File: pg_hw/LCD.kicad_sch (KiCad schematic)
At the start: 28 parts, among them J2 FPC_Touch, J3 FPC_Display, U10 ttp233, U11 ttp233, U8 ttp233, U9 TTP233

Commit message: update ttp
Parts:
- removed R17, R18, R19, R20, R21, R22, R23, R24: R, Resistor_SMD:R_0402_1005Metric, symbol Device:R
- C12, C16, C18: value C -> 100u
- C13, C15, C17, C7: value C -> 22pF
- C14: value C -> 100uF
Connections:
- net GND: now also U10.4 (AHLB), U10.6 (TOG), U11.4 (AHLB), U11.6 (TOG), U8.4 (AHLB), U8.6 (TOG), U9.4 (AHLB), U9.6 (TOG)
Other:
- moved on the sheet: C12, C14, C16, C18

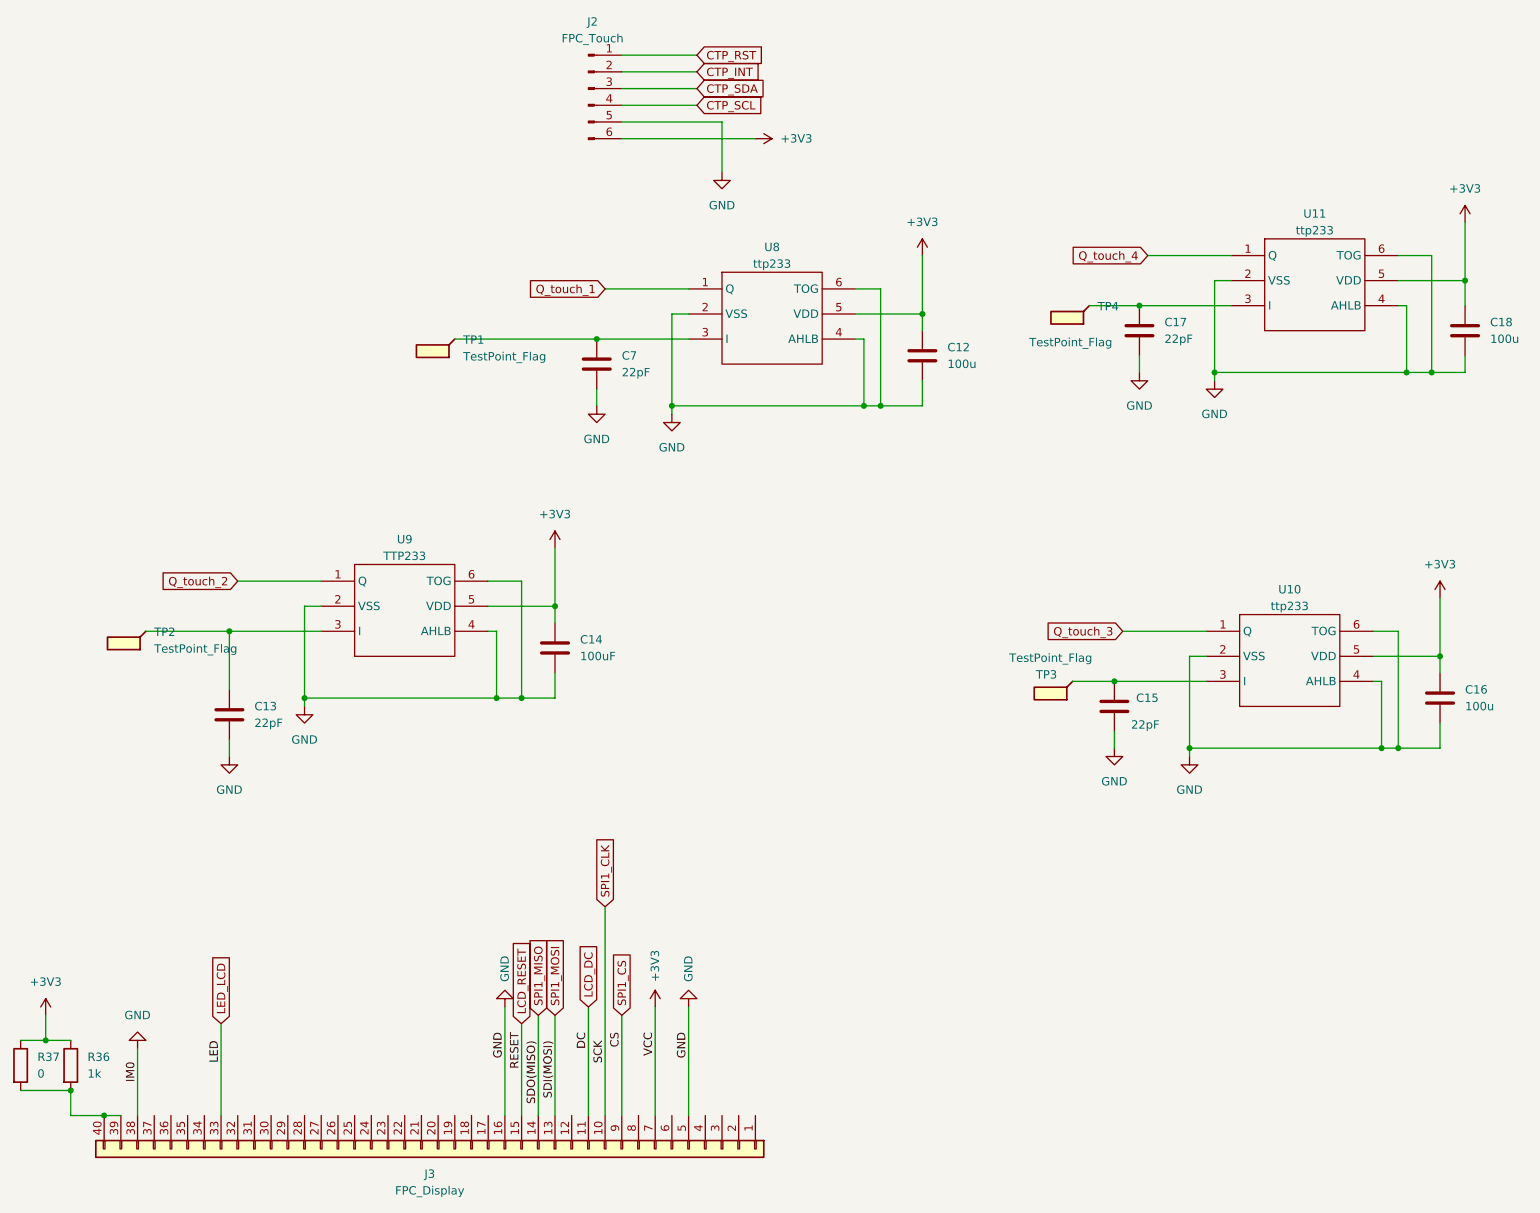
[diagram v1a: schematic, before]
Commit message: update touch pad
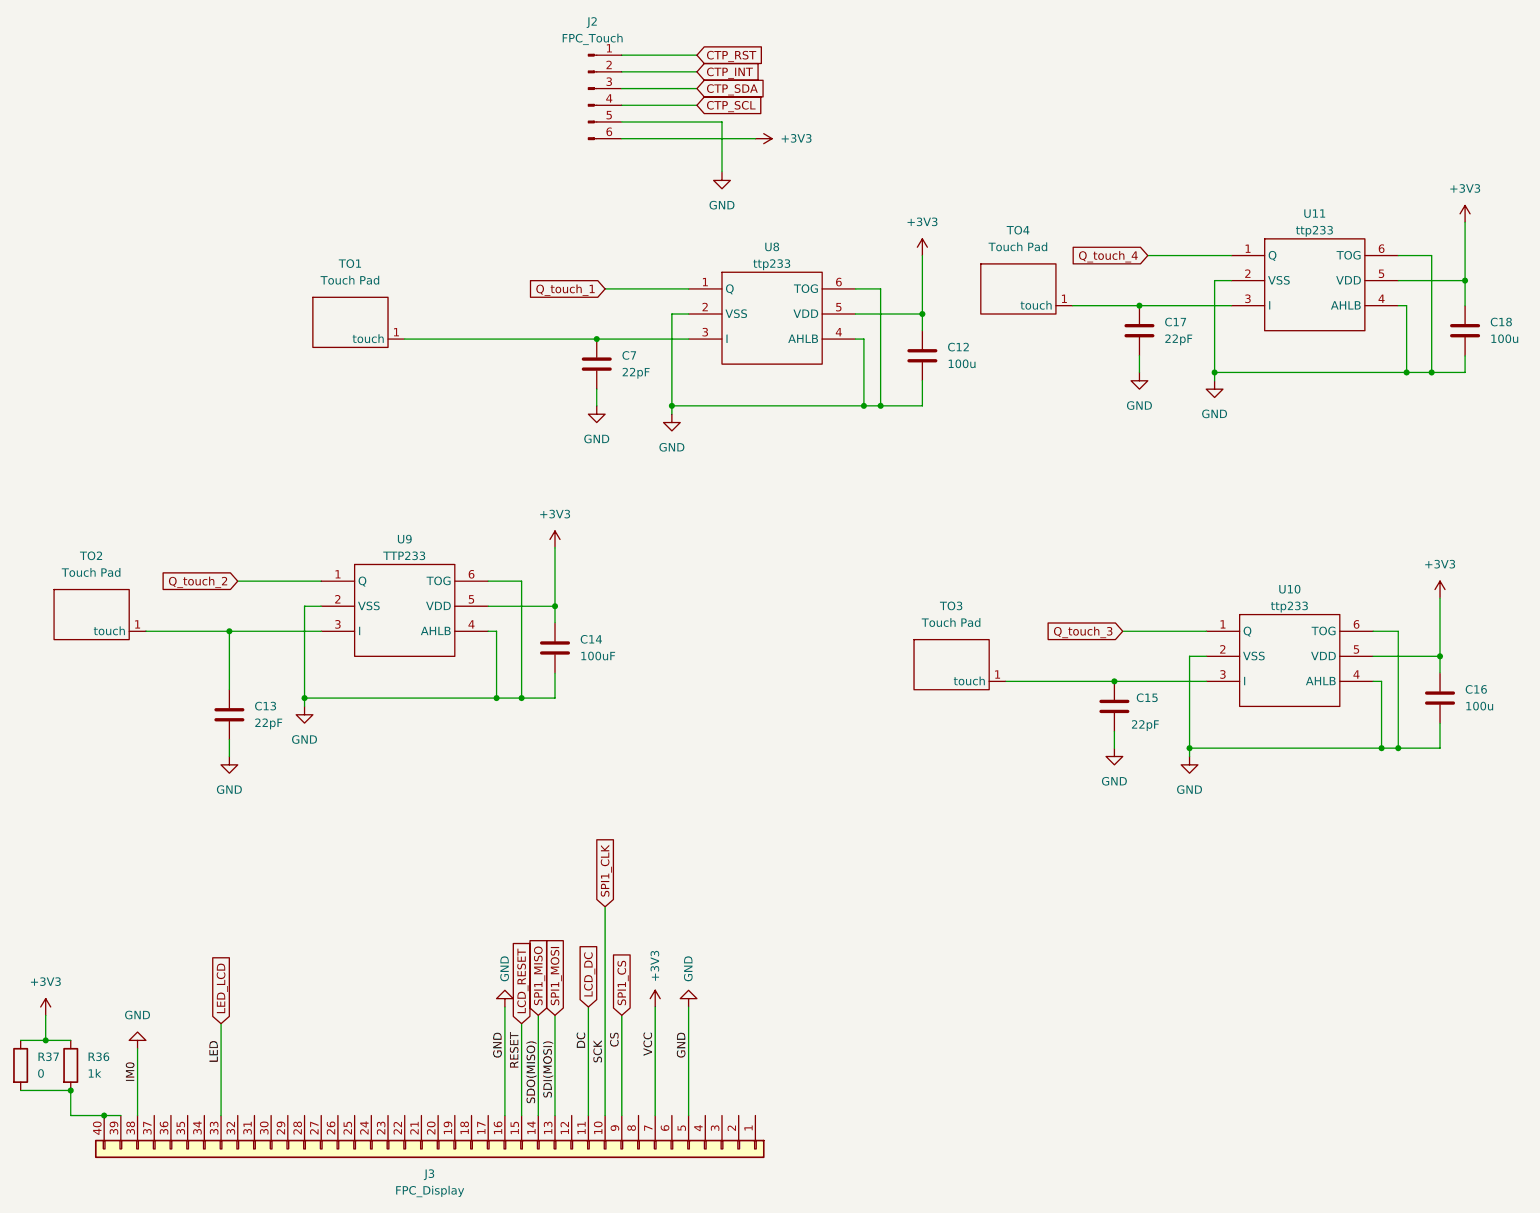
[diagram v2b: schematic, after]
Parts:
- removed TP1, TP2, TP3, TP4: TestPoint_Flag, symbol Connector:TestPoint_Flag
- added TO1, TO2, TO3, TO4: Touch Pad, TouchPad_10.0x10.0:TouchPad, symbol TTP:TouchPad
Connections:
- net at C15.1, U10.3 (I): now also TO3.1 (touch)
- net at C13.1, U9.3 (I): now also TO2.1 (touch)
- net at C7.1, U8.3 (I): now also TO1.1 (touch)
- net at C17.1, U11.3 (I): now also TO4.1 (touch)
